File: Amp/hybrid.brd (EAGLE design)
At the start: 172.7 x 137.2 mm, 125 parts, among them IC1 TL071P, IC2 TL071P, IC3 LM317MABT, IC4 LM317MABT, J2 NRJ3HF-1, Q1 KSP06KINKED, Q10 BD139, Q11 KSP06KINKED, Q12 BC560KINKED, Q13 BC560KINKED, Q14 BC560KINKED, Q15 BC556KINKED, Q16 BC550KINKED, Q17 BC550KINKED, Q18 BC560KINKED, Q19 BD140, Q2 BC560KINKED, Q20 BD139, Q21 KSP43, Q22 KSP43, Q3 BC560KINKED, Q4 BC560KINKED, Q5 BC556KINKED, Q6 BC550KINKED, Q7 BC550KINKED, Q8 BC560KINKED, Q9 BD140

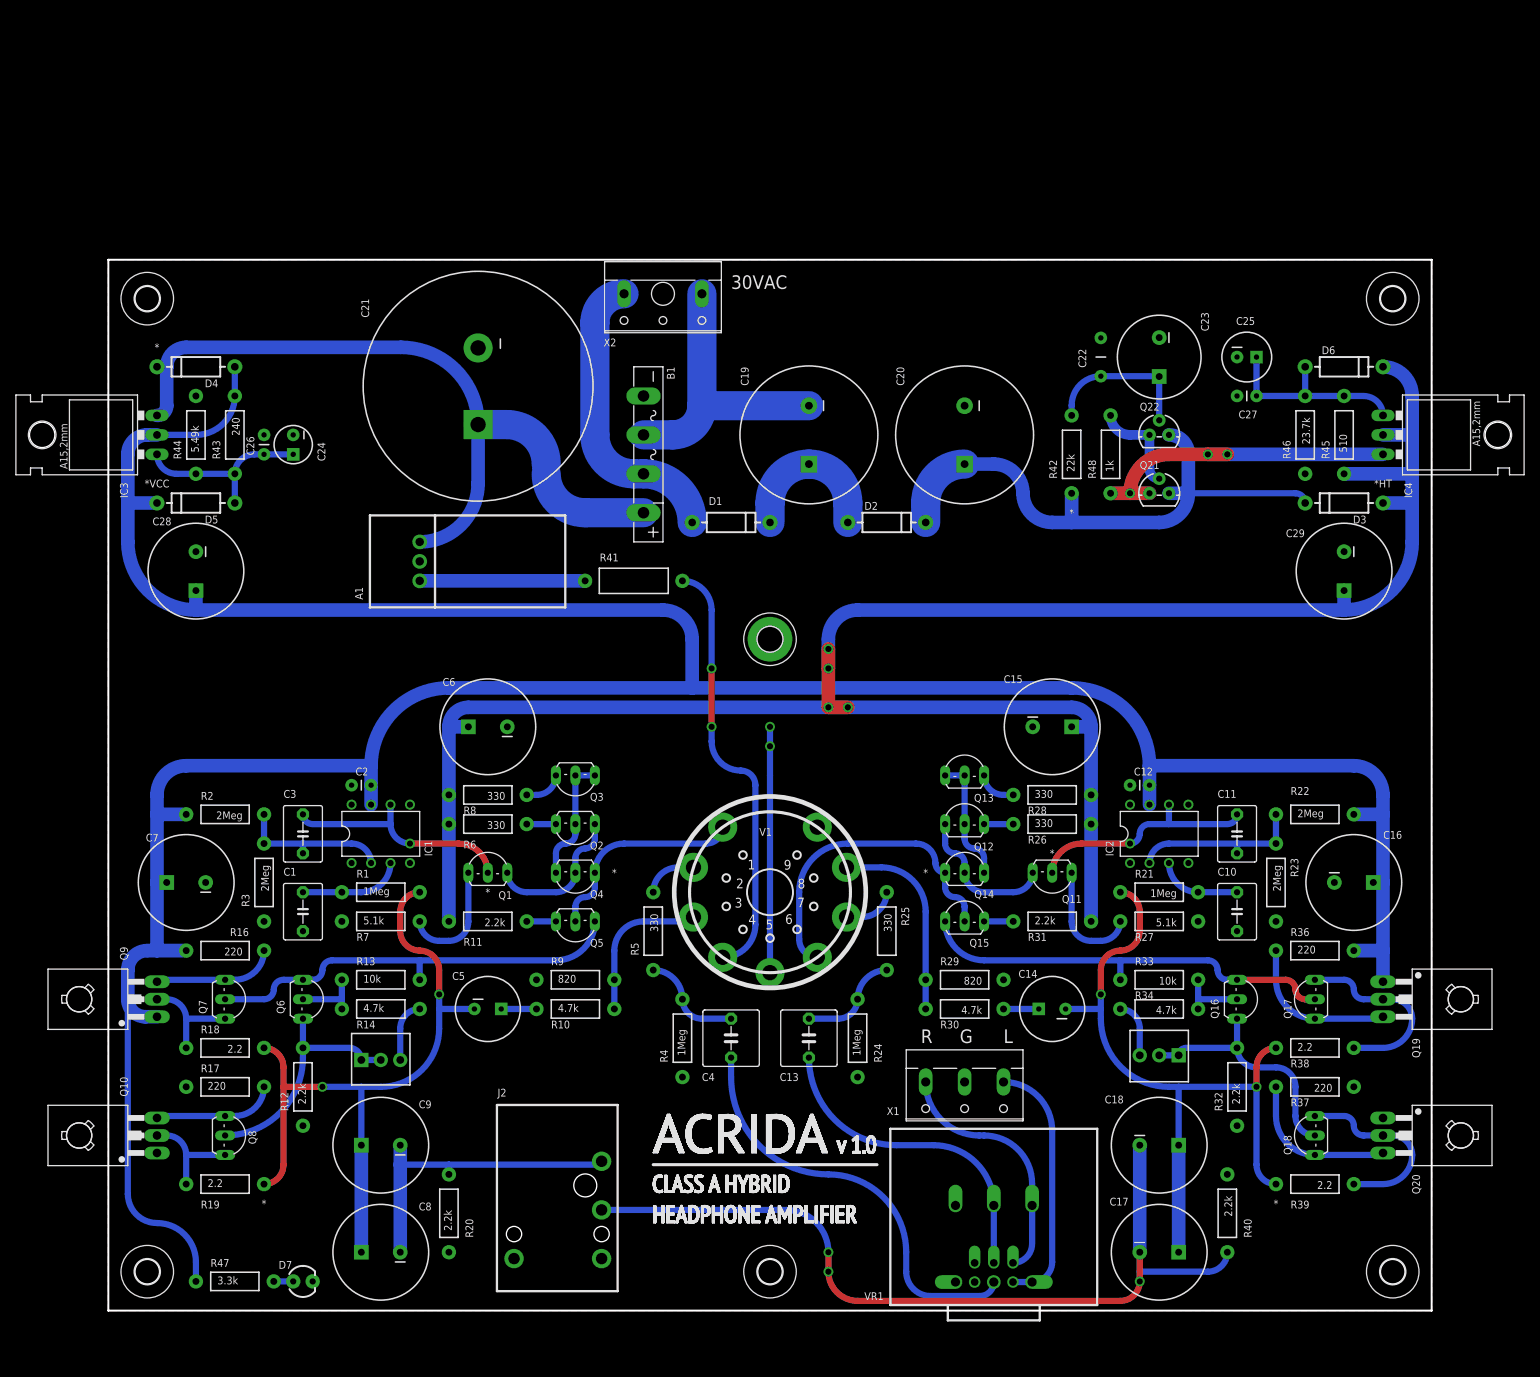
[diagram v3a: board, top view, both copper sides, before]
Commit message: Optional protection circuit
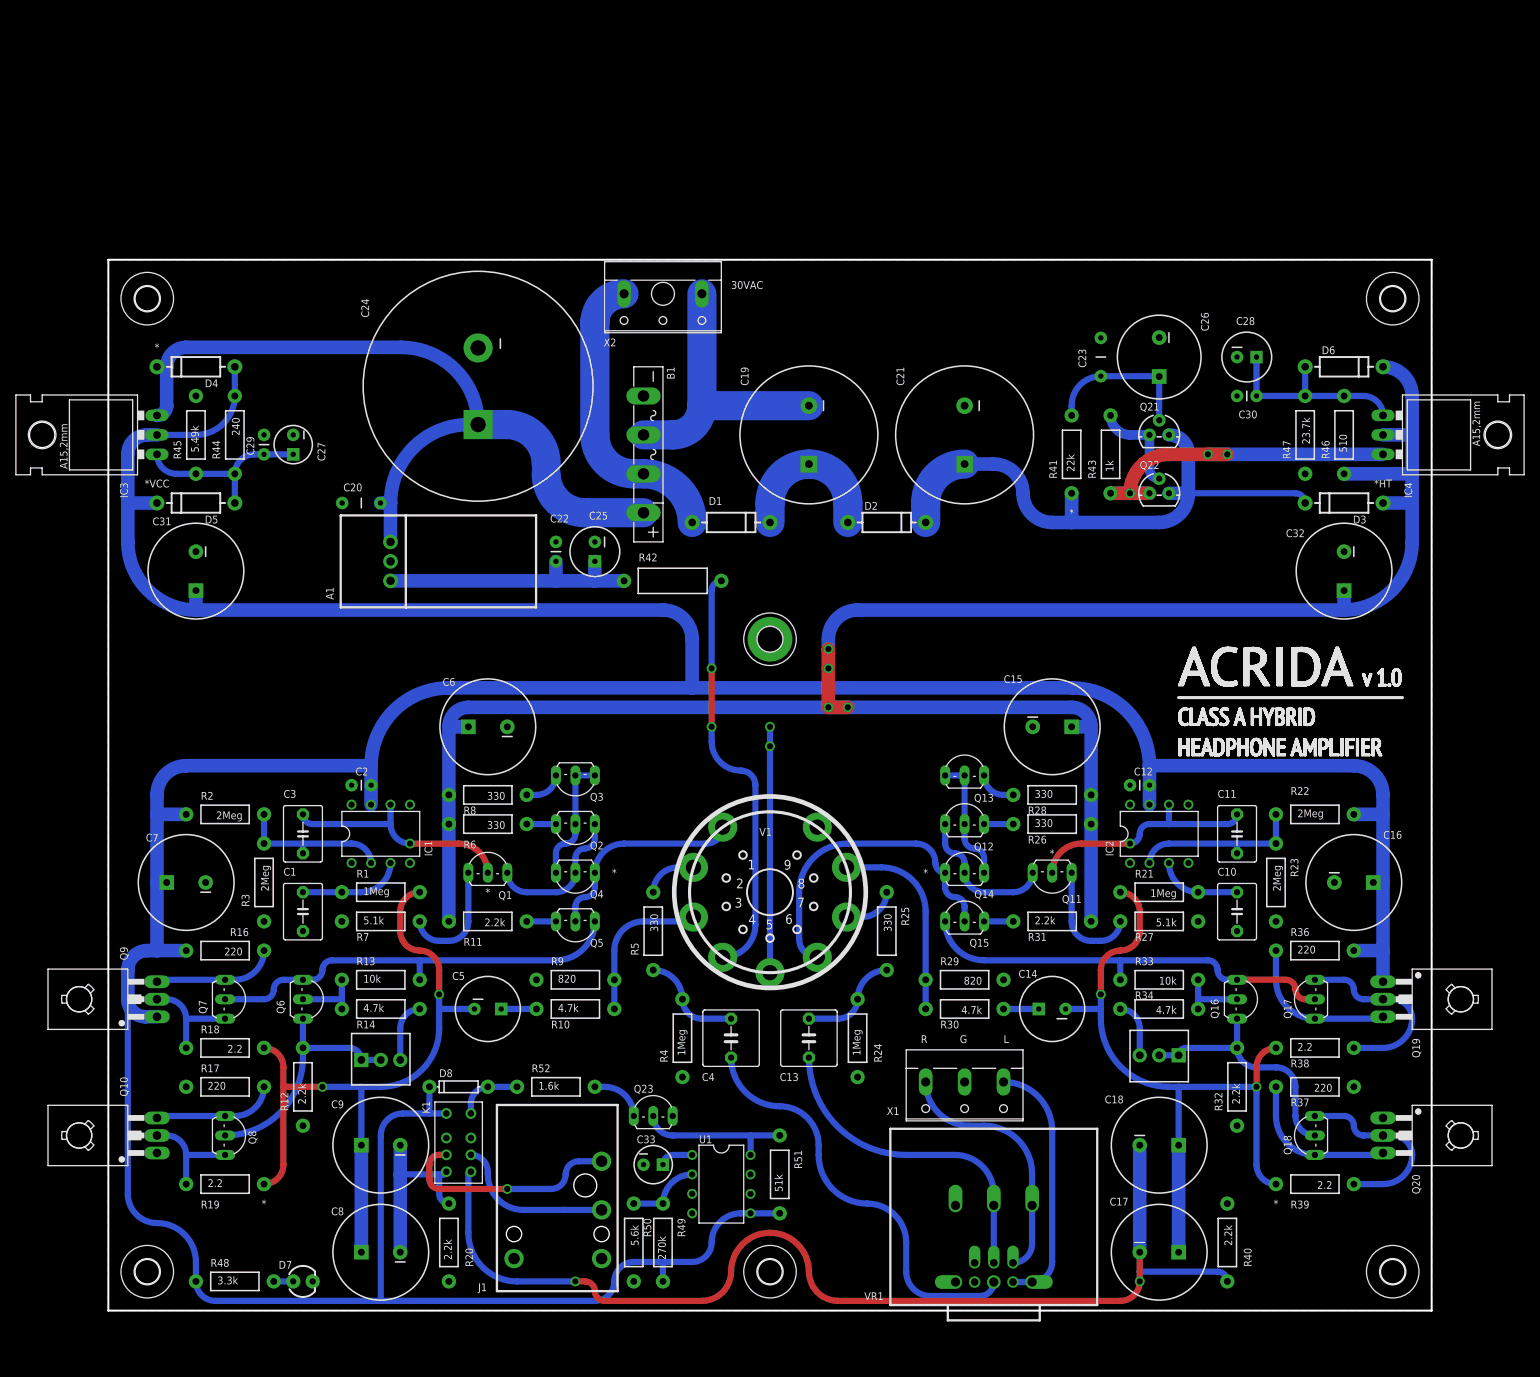
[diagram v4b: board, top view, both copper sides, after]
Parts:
- added C30: 1uF, SparkFun-Capacitors:CAP-PTH-SMALL
- added C31, C32: 100uF, my-cap:CPOL-RADIAL-12.5/5
- added C33: 10uF, my-cap:CPOL-RADIAL-5/2.5
- added D8: (no value), SparkFun-DiscreteSemi:DIODE-1N4148-KIT
- added K1: UA2-12NJ, my-relay:UA2
- added Q23: BC546KINKED, my-tran:TO92-BENT
- added R49: 270k, SparkFun-Resistors:AXIAL-0.4
- added R50: 5.6k, SparkFun-Resistors:AXIAL-0.4
- added R51: 51k, SparkFun-Resistors:AXIAL-0.4
- added R52: 1.6k, SparkFun-Resistors:AXIAL-0.4
- added U1: TL7700DIP-8, my-ic:DIL08
- C20: value 470uF -> 1uF; device my-cap:CPOL-RADIAL-18/7.5 -> SparkFun-Capacitors:CAP-PTH-5MM
- C21: value 4700uF -> 470uF; device my-cap:CPOL-SNAPIN-30/10 -> my-cap:CPOL-RADIAL-18/7.5
- C22: device SparkFun-Capacitors:CAP-PTH-5MM -> SparkFun-Capacitors:CAP-PTH-SMALL
- C23: value 10uF -> 1uF; device my-cap:CPOL-RADIAL-12/5 -> SparkFun-Capacitors:CAP-PTH-5MM
- C24: value 10uF -> 4700uF; device my-cap:CPOL-RADIAL-5/2.5 -> my-cap:CPOL-SNAPIN-30/10
- C25: value 10uF -> 100uF
- C26: value 1uF -> 10uF; device SparkFun-Capacitors:CAP-PTH-SMALL -> my-cap:CPOL-RADIAL-12/5
- C27: value 1uF -> 10uF; device SparkFun-Capacitors:CAP-PTH-SMALL -> my-cap:CPOL-RADIAL-5/2.5
- C28: value 100uF -> 10uF; device my-cap:CPOL-RADIAL-12.5/5 -> my-cap:CPOL-RADIAL-6.5/2.5
- C29: value 100uF -> 1uF; device my-cap:CPOL-RADIAL-12.5/5 -> SparkFun-Capacitors:CAP-PTH-SMALL
- R41: value 0.51 -> 22k; device my-res:AXIAL-0.5 -> SparkFun-Resistors:AXIAL-0.4
- R42: value 22k -> 0.51; device SparkFun-Resistors:AXIAL-0.4 -> my-res:AXIAL-0.5
- R43: value 240 -> 1k
- R44: value 5.49k -> 240
- R45: value 510 -> 5.49k
- R46: value 23.7k -> 510
- R47: value 3.3k -> 23.7k
- R48: value 1k -> 3.3k
- moved R47 178.1 mm to (156.2, 114.3), turned to 270 degrees
- moved R48 157.2 mm to (16.5, 3.81), turned to 0 degrees
- moved R45 149.9 mm to (11.4, 114.3)
- moved C29 141.8 mm to (20.3, 111.8), turned to 90 degrees
- moved C28 140.0 mm to (148.6, 124.5), turned to 0 degrees
- moved C27 125.9 mm to (24.1, 113.0), turned to 270 degrees
- moved C26 117.5 mm to (137.2, 124.5), turned to 270 degrees
- moved R43 114.3 mm to (130.8, 111.8), turned to 90 degrees
- moved LOGO1 91.8 mm to (139.7, 72.4)
- moved C25 88.8 mm to (63.5, 99.1), turned to 270 degrees
- moved C20 79.2 mm to (33.0, 105.4), turned to 180 degrees
- moved C22 76.0 mm to (58.4, 97.8)
- moved C21 63.8 mm to (111.8, 114.3)
- moved R41 59.5 mm to (125.7, 111.8), turned to 90 degrees
- moved R42 54.6 mm to (73.7, 95.2), turned to 0 degrees
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- renumbered J2 to J1
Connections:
- new net N$40: C33.1, U1.1
- new net N$44: Q23.2, R51.P$2, U1.8
- new net N$45: R49.P$2, R50.P$1, U1.2
- new net N$49: D8.A, K1.8, R52.P$1
- new net N$50: Q23.1, R52.P$2
- new net OUT_L*: J1.T, K1.3
- new net OUT_R*: J1.R, K1.6
- net +6.3FIL: now also R42.P$2; no longer R41.P$2
- net +LV: now also C20.1, C24.1; no longer C21.1
- net GND: now also C23.2, C26.-, C28.2, C29.2, C30.2, C31.-, C32.-, C33.2, K1.2, K1.7, Q23.3, R45.P$2, R47.P$2, R50.P$2, U1.4; no longer C23.-, C26.2, C28.-, C29.-, R44.P$2, R46.P$2
- net HT: now also C32.+, R46.P$1; no longer C29.+, R45.P$1
- net N$18: now also Q21.1, Q22.2, R43.P$2; no longer Q21.2, Q22.1, R48.P$2
- net N$30: now also C27.1, C29.1, R44.P$2, R45.P$1; no longer C24.1, C26.1, R43.P$2, R44.P$1
- net N$32: now also C22.1, C25.1, R42.P$1; no longer R41.P$1
- net N$33: now also C21.1, R41.P$1; no longer C20.1, R42.P$1
- net N$34: now also C23.1, C26.+, Q21.2, R41.P$2; no longer C22.1, C23.+, Q22.2, R42.P$2
- net N$36: now also C28.1, C30.1, R46.P$2, R47.P$1; no longer C25.1, C27.1, R45.P$2, R46.P$1
- net N$37: now also Q22.1, R43.P$1; no longer Q21.1, R48.P$1
- net N$46: now also R48.P$2; no longer R47.P$2
- net OUT_L: now also K1.4; no longer J1.T
- net OUT_R: now also K1.5; no longer J1.R
- net VCC: now also C31.+, D8.C, K1.1, R44.P$1, R48.P$1, R49.P$1, R51.P$1, U1.5; no longer C28.+, R43.P$1, R47.P$1
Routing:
- net VCC: track 422.2 -> 541.5 mm
- net OUT_L*: track 0.00 -> 29.1 mm, vias 0 -> 1
- net OUT_R: track 114.3 -> 141.4 mm, vias 3 -> 2
- net OUT_R*: track 0.00 -> 20.7 mm
- net N$44: track 0.00 -> 20.1 mm
- net OUT_L: track 41.7 -> 24.5 mm
- net N$32: track 21.6 -> 35.6 mm
- net N$45: track 0.00 -> 9.20 mm
- net N$49: track 0.00 -> 8.21 mm
- net N$50: track 0.00 -> 6.66 mm
- net N$40: track 0.00 -> 4.34 mm
- net +LV: track 99.6 -> 103.2 mm
- net +6.3FIL: track 54.8 -> 53.8 mm
- net IN_R: track 39.9 -> 40.7 mm
- net IN_R*: track 30.8 -> 31.5 mm

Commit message: Final polishing
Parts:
- C27, C33: device my-cap:CPOL-RADIAL-5/2.5 -> my-cap:CPOL-RADIAL-6.5/2.5
- moved C27 2.84 mm to (25.4, 110.5)
- moved C29 2.54 mm to (20.3, 109.2)
- turned C15 to 270 degrees
- turned C6 to 270 degrees
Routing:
- net HT: track 280.7 -> 269.0 mm
- net +LV: track 103.2 -> 97.9 mm
- net VCC: track 541.5 -> 542.8 mm
- net +6.3FIL: track 53.8 -> 52.7 mm
